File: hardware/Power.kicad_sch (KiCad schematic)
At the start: 17 parts, among them K11 G5V-2-DC12, U2 V7805-1000

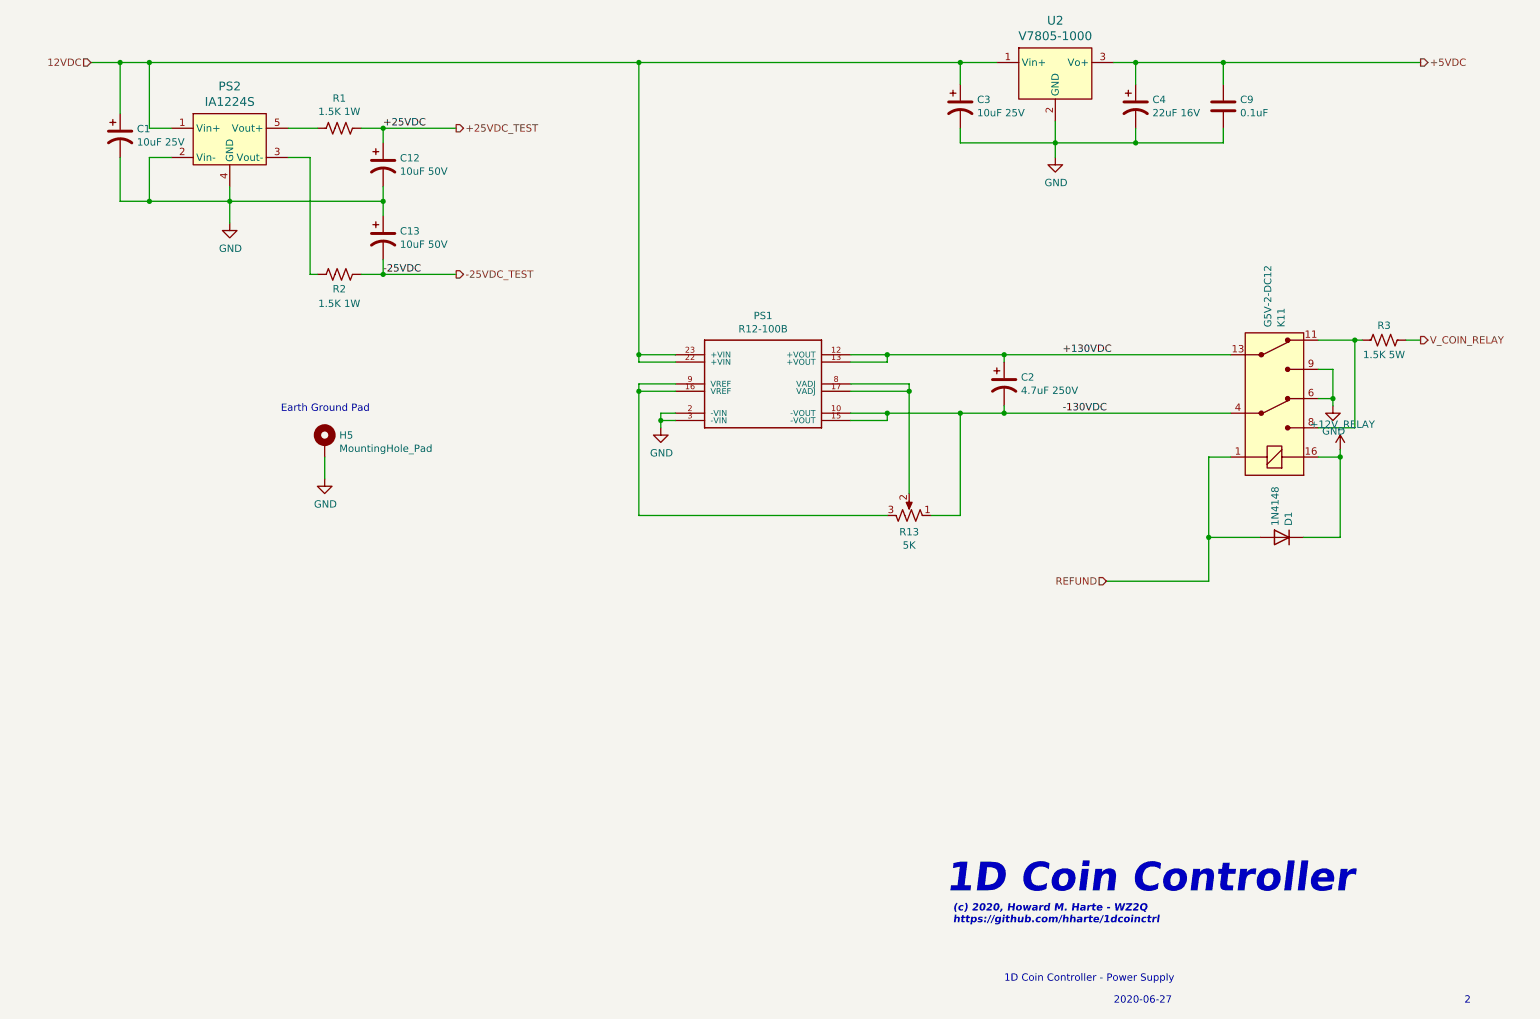
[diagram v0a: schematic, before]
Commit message: Issue 3:
* Remove barrel jack, replace with 4-position terminal block with
  provision for +/- 130VDC input in case the user already has an
  appropriate power supply and does not want the on-board
  DC-DC converter.  Note: 130V DC-DC converter PS2, relay
  K8, C14, D10, and R16 must be omitted during assembly.
* Add bi-color LEDs for line status.
  Green=Off-hook, normal polarity.
  Red=Off-hook, reverse polarity.
  Off=on-hook.
* Add header for FTDI USB UART, if user does not RS-232 UART levels.
  To use the FTDI header, do not populate U1 and other components on
  pp. 3 of the schematic.
* Remove i2c I/O expander and use PIC GPIOs directly.
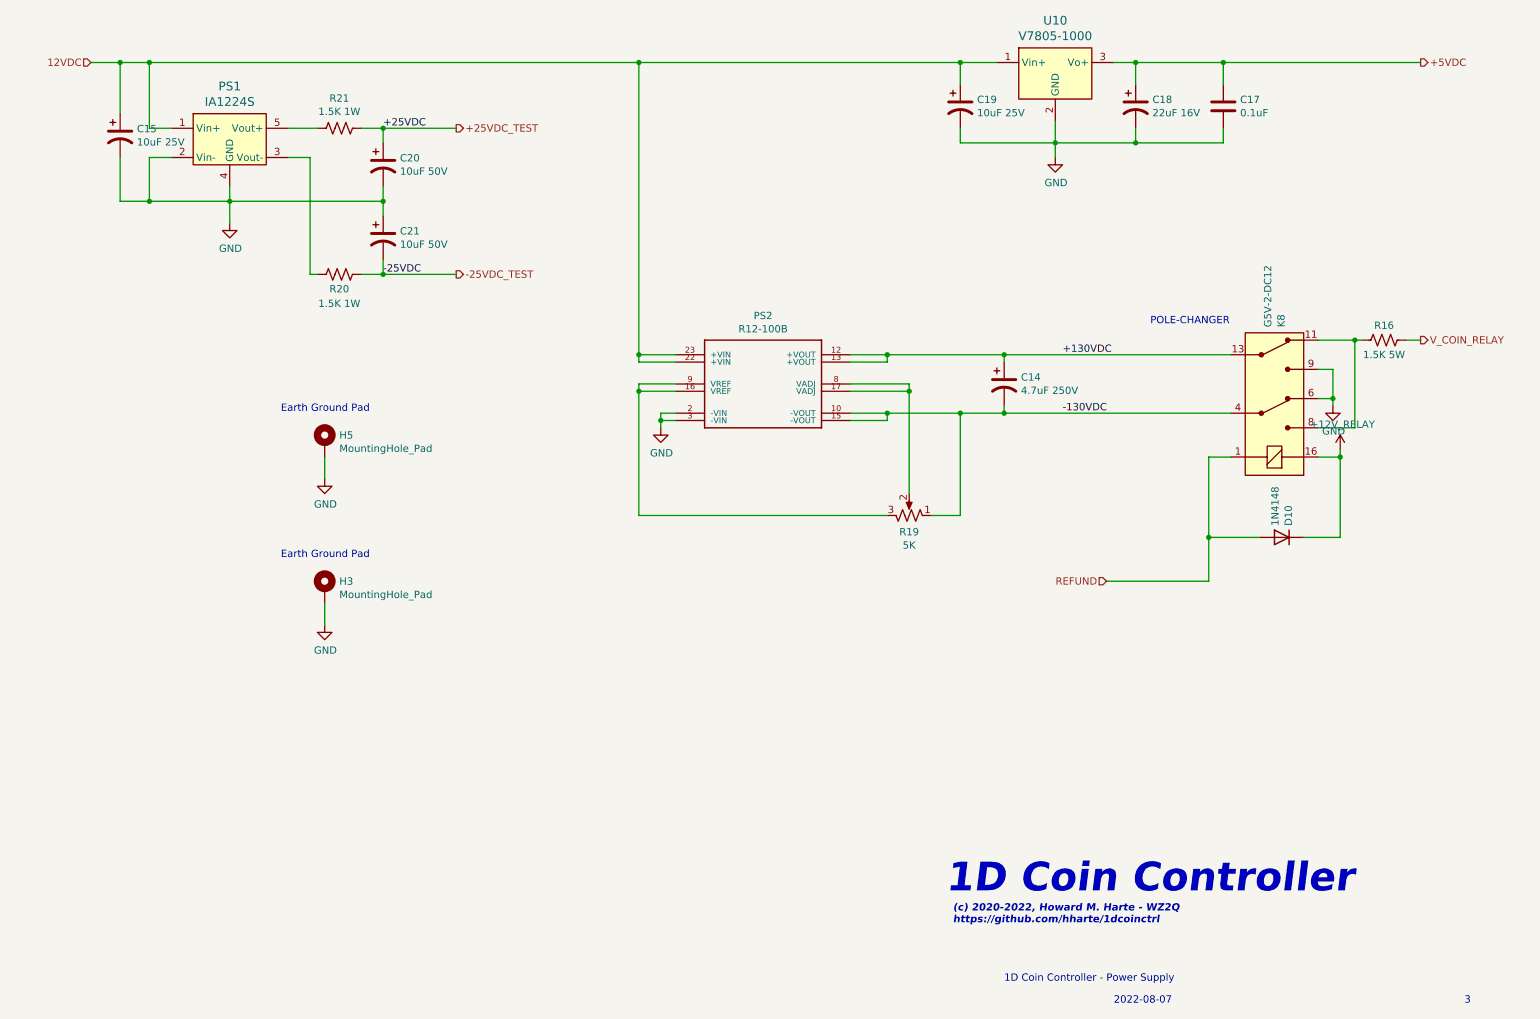
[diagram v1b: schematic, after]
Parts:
- added H3: MountingHole_Pad, MountingHole:MountingHole_3.7mm_Pad, symbol Mechanical:MountingHole_Pad
- K8: renamed from K11; Digi-Key_PN Z768-ND -> PB1125-ND
- renumbered C2 to C14, C1 to C15, C9 to C17, C4 to C18, C3 to C19, C12 to C20, C13 to C21, D1 to D10, PS2 to PS1, PS1 to PS2, R3 to R16, R13 to R19, R2 to R20, R1 to R21, U2 to U10
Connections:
- net GND: now also H3.1
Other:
- note added: "(c) 2020-2022, Howard M. Harte - WZ2Q https://github.com/hharte/1dcoinctrl"
- note added: "2022-08-07"
- note added: "3"
- note added: "POLE-CHANGER"
- note removed: "(c) 2020, Howard M. Harte - WZ2Q https://github.com/hharte/1dcoinctrl"
- note removed: "2"
- note removed: "2020-06-27"
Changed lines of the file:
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@@
+    (stroke (width 0) (type default) (color 0 0 0 0))
+  )
+  (wire (pts (xy 69.85 128.27) (xy 69.85 124.46))
     (stroke (width 0) (type default) (color 0 0 0 0))
   )
@@
     (stroke (width 0) (type default) (color 0 0 0 0))
   )
-  (text "(c) 2020, Howard M. Harte - WZ2Q\nhttps://github.com/hharte/1dcoinctrl"
+  (text "(c) 2020-2022, Howard M. Harte - WZ2Q\nhttps://github.com/hharte/1dcoinctrl"
     (at 179.07 180.34 0)
     (effects (font (size 1.27 1.27) (thickness 0.254) bold italic) (justify left bottom))
   )
+  (text "POLE-CHANGER" (at 213.36 76.2 0)
+    (effects (font (size 1.27 1.27)) (justify left bottom))
+  )
   (text "Earth Ground Pad" (at 62.23 91.44 0)
     (effects (font (size 1.27 1.27)) (justify left bottom))
   )
-  (text "2" (at 267.97 194.31 0)
+  (text "Earth Ground Pad" (at 62.23 116.84 0)
+    (effects (font (size 1.27 1.27)) (justify left bottom))
+  )
+  (text "3" (at 267.97 194.31 0)
     (effects (font (size 1.27 1.27)) (justify left bottom))
   )
@@
     (effects (font (size 1.27 1.27)) (justify left bottom))
   )
-  (text "2020-06-27" (at 207.01 194.31 0)
+  (text "2022-08-07" (at 207.01 194.31 0)
     (effects (font (size 1.27 1.27)) (justify left bottom))
   )
@@
   (symbol (lib_id "1d_coinctrl_r2-rescue:IA1224S-dk_DC-DC-Converters") (at 53.34 44.45 0) (unit 1)
     (in_bom yes) (on_board yes)
-    (property "Reference" "PS2" (id 0) (at 53.34 34.6202 0)
+    (property "Reference" "PS1" (id 0) (at 53.34 34.6202 0)
       (effects (font (size 1.524 1.524)))
     )
@@
   (symbol (lib_id "1d_coinctrl_r2-rescue:V7805-1000-dk_DC-DC-Converters") (at 196.85 33.02 0) (unit 1)
     (in_bom yes) (on_board yes)
-    (property "Reference" "U2" (id 0) (at 196.85 23.1902 0)
+    (property "Reference" "U10" (id 0) (at 196.85 23.1902 0)
       (effects (font (size 1.524 1.524)))
     )
@@
   (symbol (lib_id "Device:C_Polarized_US") (at 180.34 38.1 0) (unit 1)
     (in_bom yes) (on_board yes)
-    (property "Reference" "C3" (id 0) (at 183.261 36.9316 0)
+    (property "Reference" "C19" (id 0) (at 183.261 36.9316 0)
       (effects (font (size 1.27 1.27)) (justify left))
     )
@@
   (symbol (lib_id "Device:C_Polarized_US") (at 210.82 38.1 0) (unit 1)
     (in_bom yes) (on_board yes)
-    (property "Reference" "C4" (id 0) (at 213.741 36.9316 0)
+    (property "Reference" "C18" (id 0) (at 213.741 36.9316 0)
       (effects (font (size 1.27 1.27)) (justify left))
     )
@@
   (symbol (lib_id "1d_coinctrl_r2-rescue:G5V-2-DC12-dk_Signal-Relays-Up-to-2-Amps") (at 234.95 88.9 270) (mirror x) (unit 1)
     (in_bom yes) (on_board yes)
-    (property "Reference" "K11" (id 0) (at 236.1184 76.5048 0)
+    (property "Reference" "K8" (id 0) (at 236.1184 76.5048 0)
       (effects (font (size 1.27 1.27)) (justify left))
     )
@@
       (effects (font (size 1.524 1.524)) (justify left) hide)
     )
-    (property "Digi-Key_PN" "Z768-ND" (id 4) (at 245.11 83.82 0)
+    (property "Digi-Key_PN" "PB1125-ND" (id 4) (at 245.11 83.82 0)
       (effects (font (size 1.524 1.524)) (justify left) hide)
     )
@@
   (symbol (lib_id "Diode:1N4148") (at 236.22 113.03 0) (mirror y) (unit 1)
     (in_bom yes) (on_board yes)
-    (property "Reference" "D1" (id 0) (at 237.3884 111.0234 90)
+    (property "Reference" "D10" (id 0) (at 237.3884 111.0234 90)
       (effects (font (size 1.27 1.27)) (justify left))
     )
@@
   (symbol (lib_id "1d_coinctrl_r2-rescue:R12-100B-R12-100B") (at 146.05 86.36 0) (unit 1)
     (in_bom yes) (on_board yes)
-    (property "Reference" "PS1" (id 0) (at 146.05 74.4982 0))
+    (property "Reference" "PS2" (id 0) (at 146.05 74.4982 0))
     (property "Value" "R12-100B" (id 1) (at 146.05 76.8096 0))
     (property "Footprint" "kicad-snapeda:CONV_R12-100B" (id 2) (at 146.05 86.36 0)
@@
   (symbol (lib_id "Device:C_Polarized_US") (at 187.96 86.36 0) (unit 1)
     (in_bom yes) (on_board yes)
-    (property "Reference" "C2" (id 0) (at 190.881 85.1916 0)
+    (property "Reference" "C14" (id 0) (at 190.881 85.1916 0)
       (effects (font (size 1.27 1.27)) (justify left))
     )
@@
   (symbol (lib_id "Device:R_US") (at 254 78.74 270) (unit 1)
     (in_bom yes) (on_board yes)
-    (property "Reference" "R3" (id 0) (at 254 76.2 90))
+    (property "Reference" "R16" (id 0) (at 254 76.2 90))
     (property "Value" "1.5K 5W" (id 1) (at 254 81.28 90))
     (property "Footprint" "Resistor_THT:R_Axial_Power_L25.0mm_W9.0mm_P30.48mm" (id 2) (at 253.746 79.756 90)
@@
   (symbol (lib_id "Device:C_Polarized_US") (at 34.29 43.18 0) (unit 1)
     (in_bom yes) (on_board yes)
-    (property "Reference" "C1" (id 0) (at 37.211 42.0116 0)
+    (property "Reference" "C15" (id 0) (at 37.211 42.0116 0)
       (effects (font (size 1.27 1.27)) (justify left))
     )
@@
   (symbol (lib_id "Device:R_Potentiometer_US") (at 171.45 109.22 270) (mirror x) (unit 1)
     (in_bom yes) (on_board yes)
-    (property "Reference" "R13" (id 0) (at 171.45 112.0902 90))
+    (property "Reference" "R19" (id 0) (at 171.45 112.0902 90))
     (property "Value" "5K" (id 1) (at 171.45 114.4016 90))
     (property "Footprint" "Potentiometer_THT:Potentiometer_Bourns_3266W_Vertical" (id 2) (at 171.45 109.22 0)
@@
   (symbol (lib_id "Device:C") (at 226.06 38.1 0) (unit 1)
     (in_bom yes) (on_board yes)
-    (property "Reference" "C9" (id 0) (at 228.981 36.9316 0)
+    (property "Reference" "C17" (id 0) (at 228.981 36.9316 0)
       (effects (font (size 1.27 1.27)) (justify left))
     )
@@
   (symbol (lib_id "Device:R_US") (at 72.39 41.91 270) (unit 1)
     (in_bom yes) (on_board yes)
-    (property "Reference" "R1" (id 0) (at 72.39 36.703 90))
+    (property "Reference" "R21" (id 0) (at 72.39 36.703 90))
     (property "Value" "1.5K 1W" (id 1) (at 72.39 39.0144 90))
     (property "Footprint" "Resistor_THT:R_Axial_DIN0207_L6.3mm_D2.5mm_P10.16mm_Horizontal" (id 2) (at 72.136 42.926 90)
@@
   (symbol (lib_id "Device:R_US") (at 72.39 67.31 270) (unit 1)
     (in_bom yes) (on_board yes)
-    (property "Reference" "R2" (id 0) (at 72.39 69.85 90))
+    (property "Reference" "R20" (id 0) (at 72.39 69.85 90))
     (property "Value" "1.5K 1W" (id 1) (at 72.39 72.39 90))
     (property "Footprint" "Resistor_THT:R_Axial_DIN0207_L6.3mm_D2.5mm_P10.16mm_Horizontal" (id 2) (at 72.136 68.326 90)
@@
   (symbol (lib_id "Device:C_Polarized_US") (at 80.01 48.26 0) (unit 1)
     (in_bom yes) (on_board yes)
-    (property "Reference" "C12" (id 0) (at 82.931 47.0916 0)
+    (property "Reference" "C20" (id 0) (at 82.931 47.0916 0)
       (effects (font (size 1.27 1.27)) (justify left))
     )
@@
   (symbol (lib_id "Device:C_Polarized_US") (at 80.01 60.96 0) (unit 1)
     (in_bom yes) (on_board yes)
-    (property "Reference" "C13" (id 0) (at 82.931 59.7916 0)
+    (property "Reference" "C21" (id 0) (at 82.931 59.7916 0)
       (effects (font (size 1.27 1.27)) (justify left))
     )
@@
       (effects (font (size 1.27 1.27)) hide)
     )
+    (pin "1")
+  )
+  (symbol (lib_id "Mechanical:MountingHole_Pad") (at 69.85 121.92 0) (unit 1)
+    (in_bom yes) (on_board yes)
+    (property "Reference" "H3" (id 0) (at 72.39 120.6754 0)
+      (effects (font (size 1.27 1.27)) (justify left))
+    )
+    (property "Value" "MountingHole_Pad" (id 1) (at 72.39 122.9868 0)
+      (effects (font (size 1.27 1.27)) (justify left))
+    )
+    (property "Footprint" "MountingHole:MountingHole_3.7mm_Pad" (id 2) (at 69.85 121.92 0)
+      (effects (font (size 1.27 1.27)) hide)
+    )
+    (property "Datasheet" "~" (id 3) (at 69.85 121.92 0)
+      (effects (font (size 1.27 1.27)) hide)
+    )
+    (pin "1")
+  )
+  (symbol (lib_id "power:GND") (at 69.85 128.27 0) (unit 1)
+    (in_bom yes) (on_board yes)
+    (property "Reference" "#PWR0127" (id 0) (at 69.85 134.62 0)
+      (effects (font (size 1.27 1.27)) hide)
+    )
+    (property "Value" "GND" (id 1) (at 69.977 132.6642 0))
+    (property "Footprint" "" (id 2) (at 69.85 128.27 0)
+      (effects (font (size 1.27 1.27)) hide)
+    )
+    (property "Datasheet" "" (id 3) (at 69.85 128.27 0)
+      (effects (font (size 1.27 1.27)) hide)
+    )

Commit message: Issue 4: Switch from PIC to AVR128DA28 MCU.
    * The AVR128DA28 is supported by the Arduino IDE.
    * Simpler UPDI programming.
    * Update to KiCAD 8.0.1
    * Fix footprint outline for IA1224S DC-DC converter.
    * Add initial Arduino firmware for AVR128DA28 MCU.
    * Move Earth Ground hole.
    * Add jumpers for UART and UPDI configuration.
    * Add 3D-printable end caps for Hammond enclosure.
    * Geographical reannotate PCB.
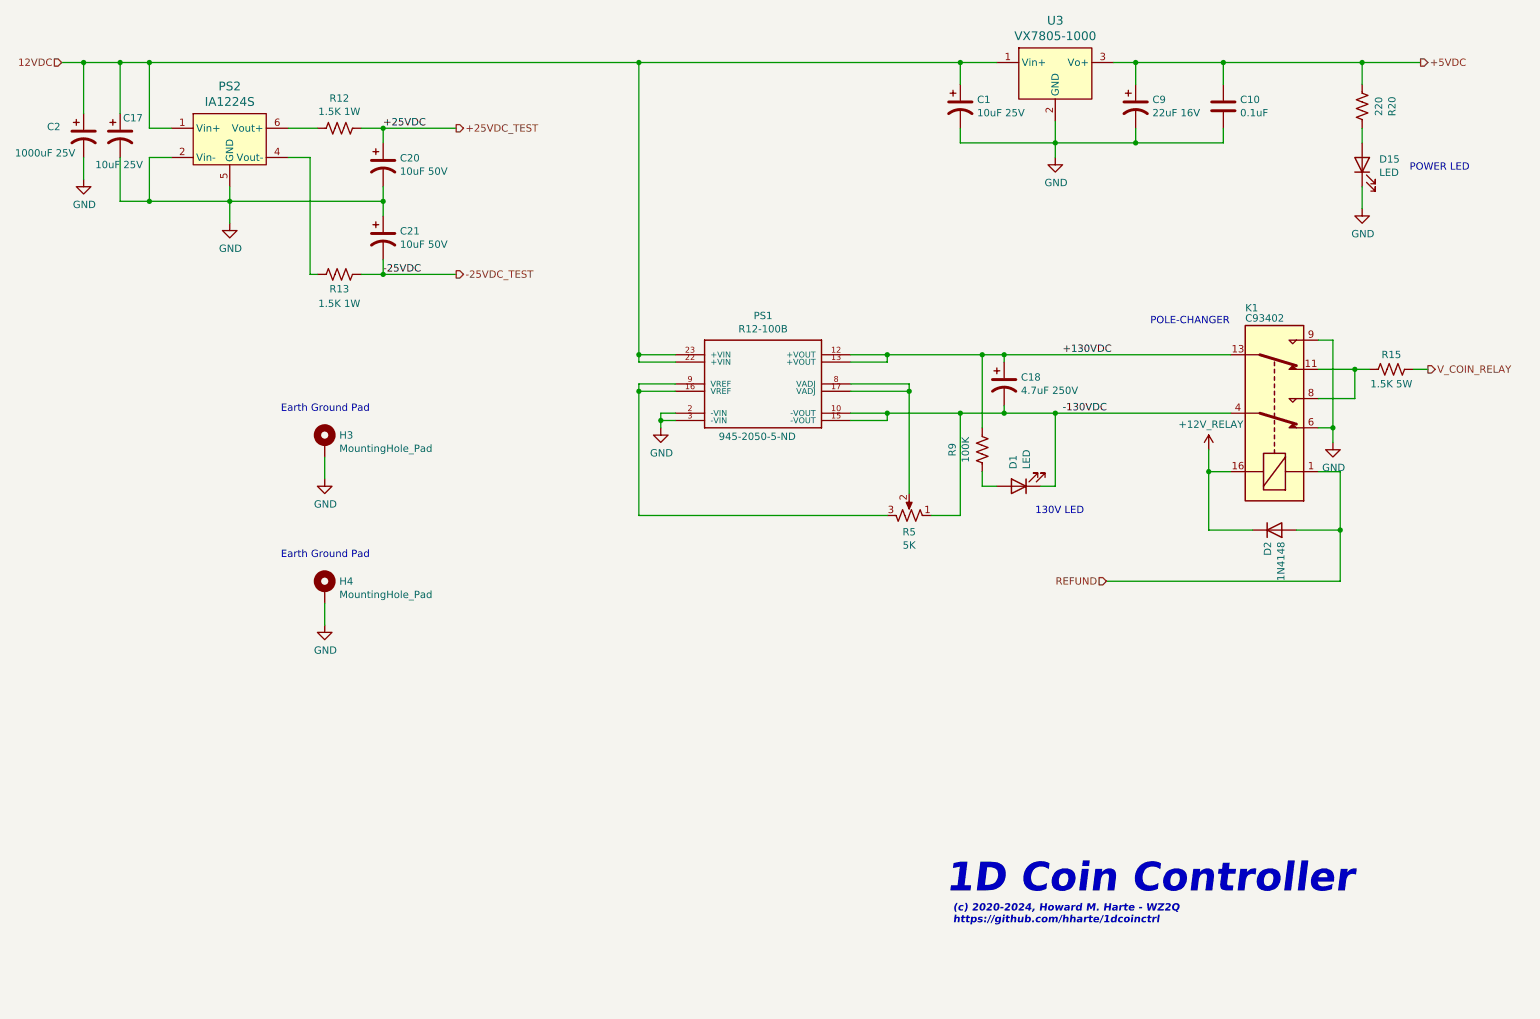
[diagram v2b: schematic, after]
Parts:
- added C2: 1000uF 25V, Capacitor_THT:CP_Radial_D12.5mm_P5.00mm, symbol Device:C_Polarized_US
- added D1, D15: LED, LED_THT:LED_D5.0mm, symbol Device:LED
- added R20: 220, Resistor_THT:R_Axial_DIN0207_L6.3mm_D2.5mm_P7.62mm_Horizontal, symbol Device:R_US
- added R9: 100K, Resistor_THT:R_Axial_DIN0207_L6.3mm_D2.5mm_P7.62mm_Horizontal, symbol Device:R_US
- C1: renamed from C19; Digi-Key_PN (none) -> 445-180683-1-ND; MPN (none) -> FA26X7R1E106KRU06
- C10: renamed from C17; Digi-Key_PN (none) -> 56-K104M15X7RF5TL2CT-ND; MPN (none) -> K104M15X7RF5TL2
- C17: renamed from C15; Digi-Key_PN (none) -> 445-180683-1-ND; MPN (none) -> FA26X7R1E106KRU06
- C18: renamed from C14; Digi-Key_PN (none) -> 338-2361-ND; MPN (none) -> SEK4R7M250ST
- C20, C21: Digi-Key_PN (none) -> P19534CT-ND; MPN (none) -> ECA-1JM100I
- C9: renamed from C18; Digi-Key_PN (none) -> 445-FK20X7R1C226MR000-ND; MPN (none) -> FK20X7R1C226MR000
- D2: renamed from D10; Digi-Key_PN (none) -> 1N4148TACT-ND; MPN (none) -> 1N4148TA
- H3: renamed from H5; now left out of the parts list
- H4: renamed from H3; now left out of the parts list
- K1: renamed from K8; value G5V-2-DC12 -> C93402; footprint digikey-footprints:Relay_THT_G5V-2 -> Relay_THT:Relay_DPDT_Omron_G5V-2; symbol 1d_coinctrl_r2-rescue:G5V-2-DC12-dk_Signal-Relays-Up-to-2-Amps -> Relay:G5V-2; DK_Datasheet_Link http://omronfs.omron.com/en_US/ecb/products/pdf/en-g5v_2.pdf -> https://omronfs.omron.com/en_US/ecb/products/pdf/en-g5v_2.p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; MPN G5V-2-DC12 -> C93402
- PS1: renamed from PS2; footprint kicad-snapeda:CONV_R12-100B -> 1dcoinctrl:CONV_R12-100B; Digi-Key_PN (none) -> 945-2050-5-ND; MPN (none) -> R12-100B
- PS2: renamed from PS1; footprint 1dcoinctrl_r2:IA1224S -> 1dcoinctrl:IA1224S; DK_Datasheet_Link https://www.cui.com/product/resource/digikeypdf/v78-500.pdf -> https://www.xppower.com/portals/0/pdfs/SF_IA.pdf; DK_Detail_Page /product-detail/en/cui-inc/V7805-500/102-1709-ND/1828602 -> https://www.digikey.com/en/products/detail/xp-power/IA1224S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; Digi-Key_PN 102-1709-ND -> 1470-1364-5-ND; MPN V7805-500 -> IA1224S; Manufacturer CUI Inc. -> XP Power
- R12: renamed from R21; Digi-Key_PN (none) -> PPC1.5KW-1CT-ND; MPN (none) -> PR01000101501JR500
- R13: renamed from R20; Digi-Key_PN (none) -> PPC1.5KW-1CT-ND; MPN (none) -> PR01000101501JR500
- R15: renamed from R16; Digi-Key_PN (none) -> A131371CT-ND; MPN (none) -> EP5WS1K5J
- R5: renamed from R19; Digi-Key_PN (none) -> 987-1067-ND; MPN (none) -> 64WR5KLF
- U3: renamed from U10; value V7805-1000 -> VX7805-1000; footprint digikey-footprints:3-SIP_Module_V7805-1000 -> 1dcoinctrl:VX7805-1000; Digi-Key_PN 102-1715-ND -> 102-4253-ND; MPN V7805-1000 -> VX7805-1000
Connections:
- net +130VDC: now also R9.1
- net +5VDC: now also R20.2
- net -130VDC: now also D1.1 (K)
- net 12VDC: now also C2.1
- net GND: now also PS2.5 (GND), C2.2, D15.1 (K); no longer PS2.4 (GND)
- net at R13.2: now also PS2.4 (Vout-); no longer PS2.3 (Vout-)
- net at R12.2: now also PS2.6 (Vout+); no longer PS2.5 (Vout+)
- new net: D1.2 (A), R9.2
- new net: D15.2 (A), R20.1
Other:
- note added: "(c) 2020-2024, Howard M. Harte - WZ2Q https://github.com/hharte/1dcoinctrl"
- note added: "130V LED"
- note added: "POWER LED"
- note removed: "(c) 2020-2022, Howard M. Harte - WZ2Q https://github.com/hharte/1dcoinctrl"
- note removed: "1D Coin Controller - Power Supply"
- note removed: "2022-08-07"
- note removed: "3"
- title: (none) -> 1D Coin Controller - Power Supply
- moved on the sheet: D2, R15
